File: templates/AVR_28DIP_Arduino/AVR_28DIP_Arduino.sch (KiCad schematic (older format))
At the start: 9 parts

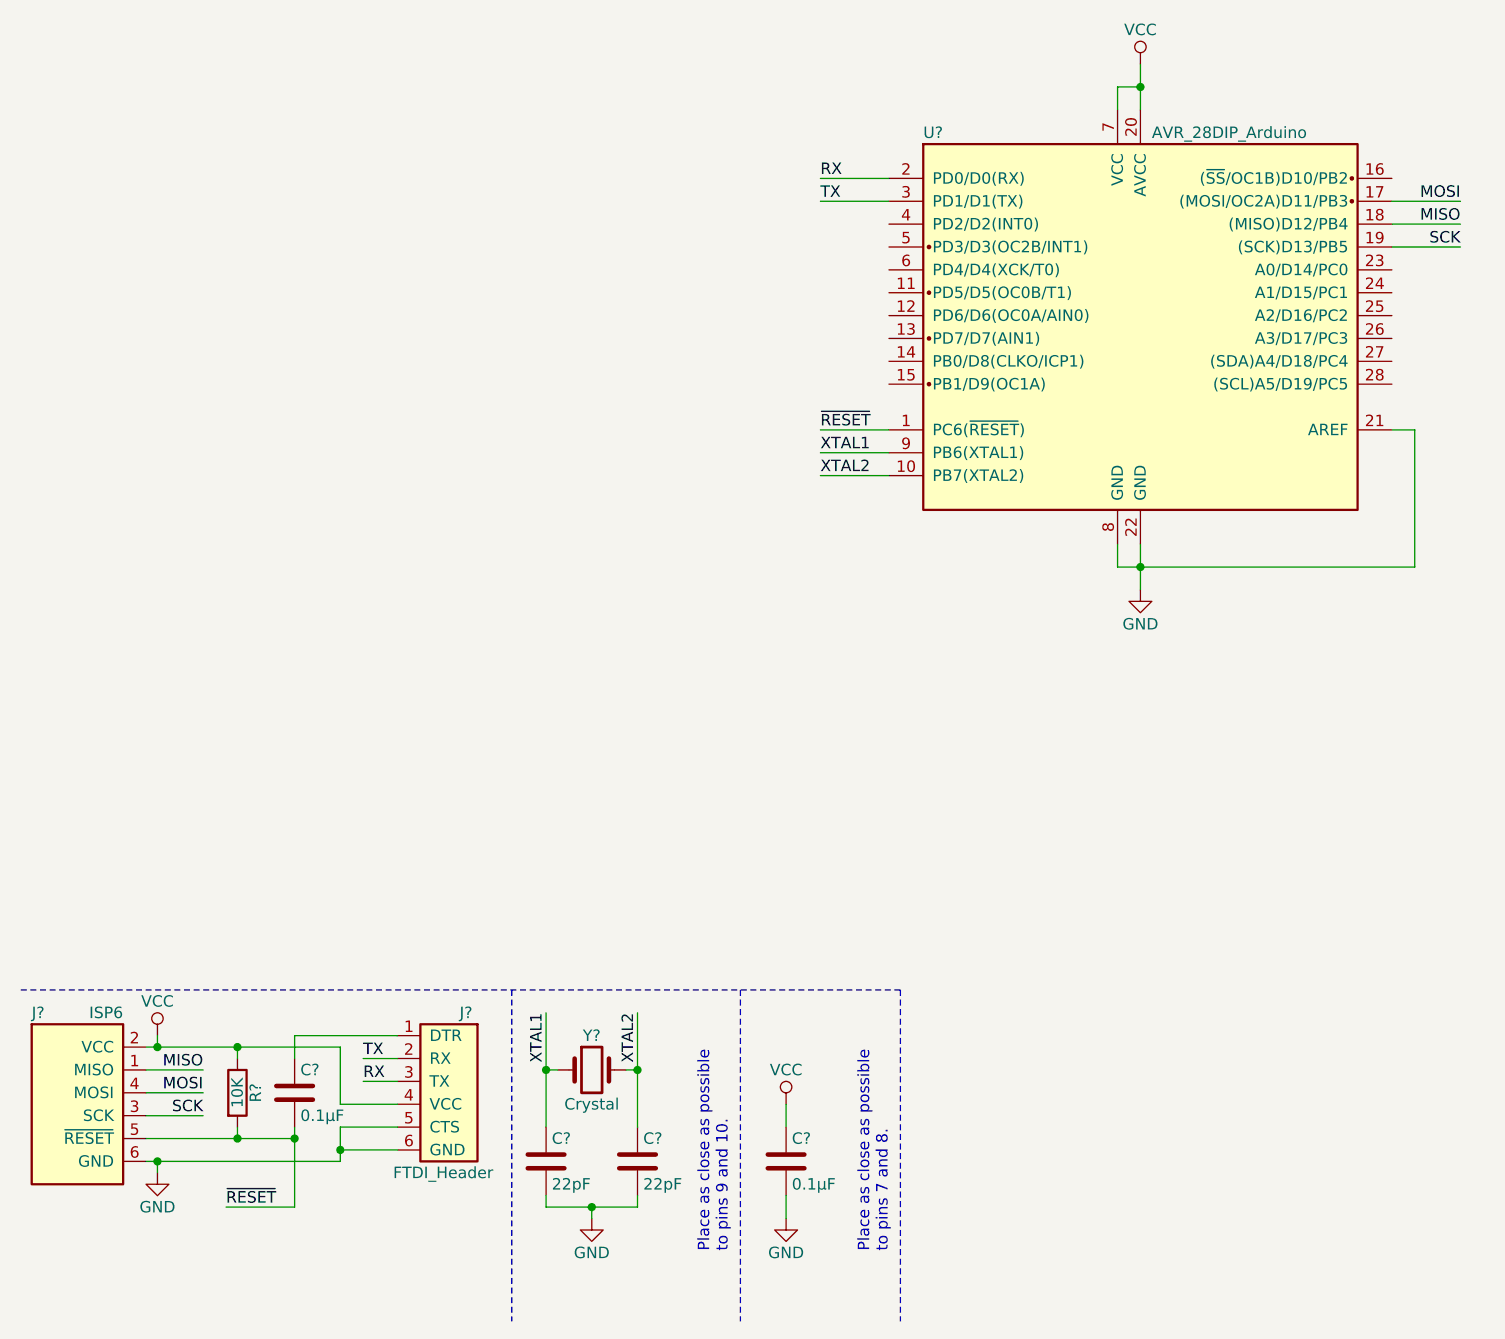
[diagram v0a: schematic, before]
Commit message: Add a capacitor between AREF and GND.  Also, make AREF Passive.
See this discussion:
https://forum.kicad.info/t/barebones-atmega328-circuit-and-the-conflict-between-pins-warning/10886
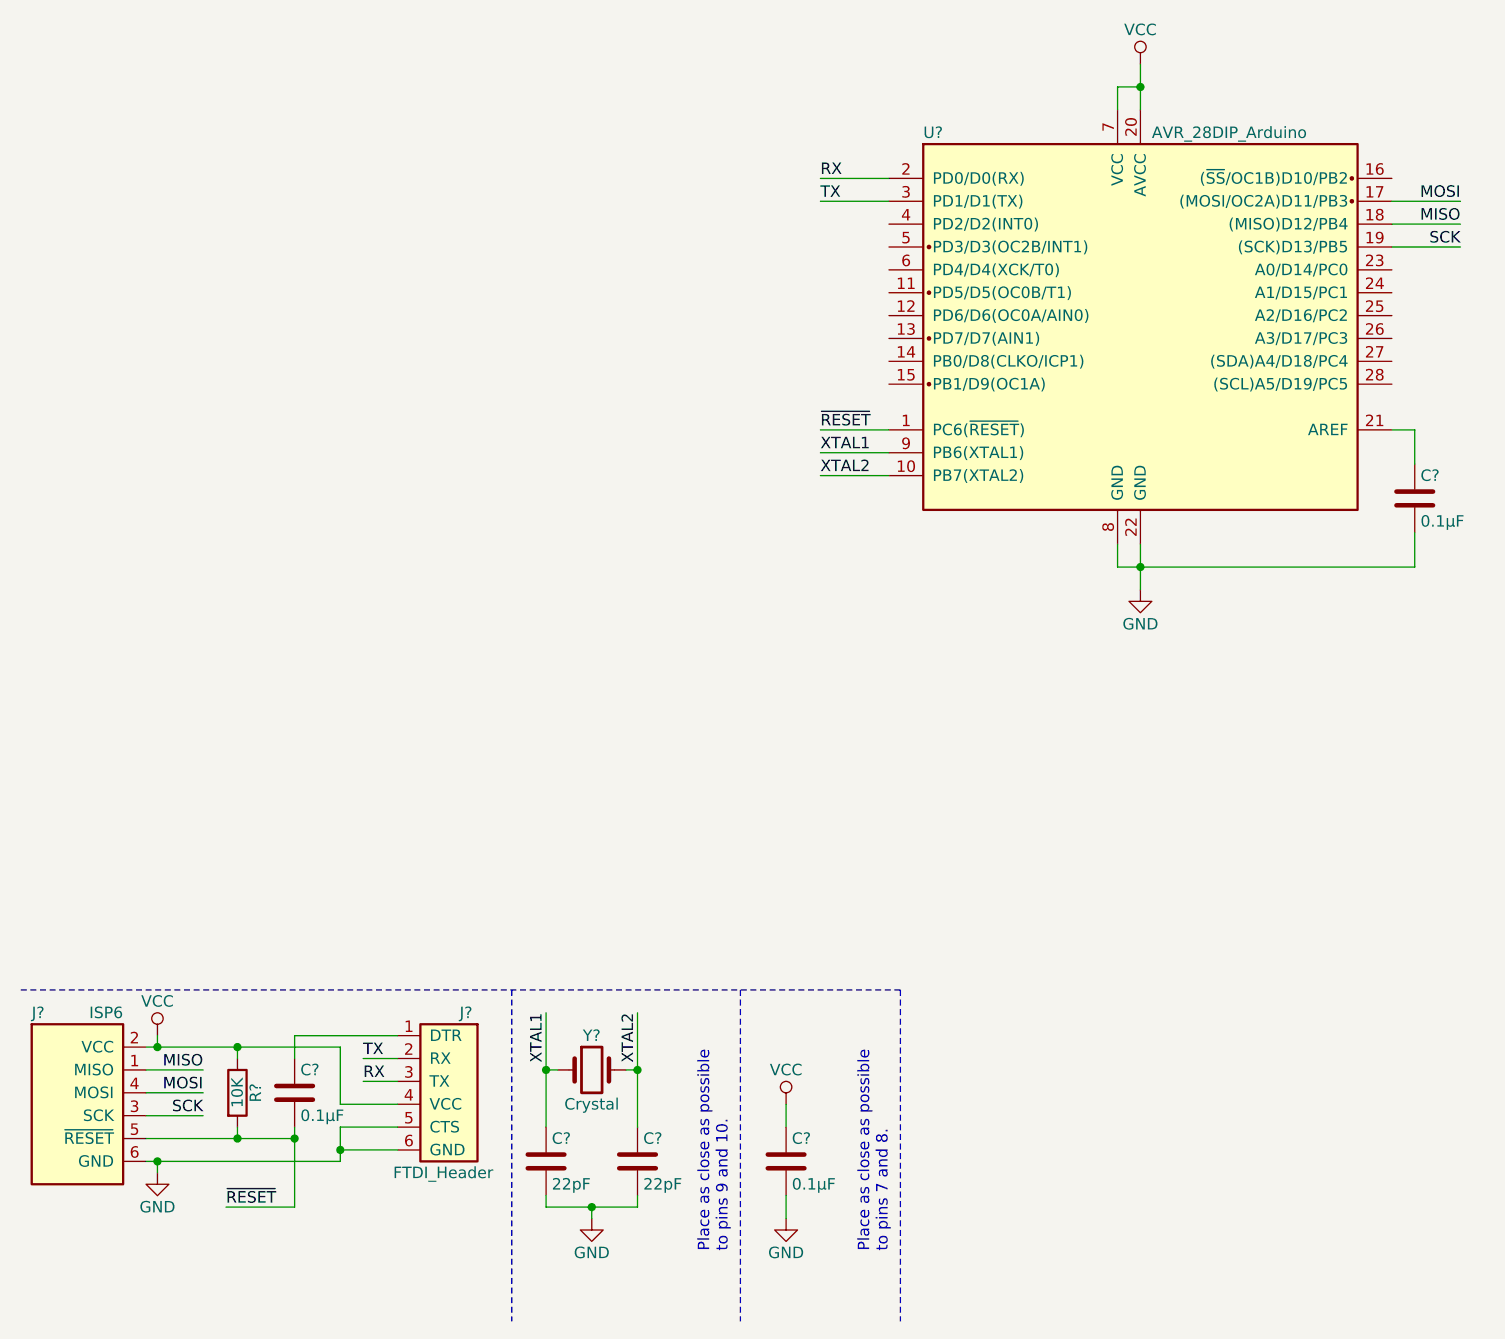
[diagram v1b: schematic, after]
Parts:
- added C?: 0.1μF, symbol C
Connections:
- net GND: now also C?.2; no longer U?.21 (AREF)
- new net: C?.1, U?.21 (AREF)
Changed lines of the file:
@@
 ~RESET
 Wire Wire Line
-	1050 6800 1100 6800
-Wire Wire Line
-	1100 6800 1450 6800
-Wire Wire Line
-	1450 6800 1900 6800
+	1050 6800 1900 6800
 Wire Wire Line
 	1100 6800 1100 6750
 Wire Wire Line
-	1050 7300 1100 7300
-Wire Wire Line
-	1100 7300 1900 7300
+	1900 7300 1050 7300
 Wire Wire Line
 	1100 7300 1100 7350
@@
 	2000 6950 2150 6950
 Wire Wire Line
-	1050 7200 1450 7200
-Wire Wire Line
-	1450 7200 1700 7200
+	1050 7200 1700 7200
 Wire Wire Line
 	1450 7200 1450 7150
@@
 Connection ~ 1100 6800
 Wire Wire Line
-	1700 7150 1700 7200
-Wire Wire Line
-	1700 7200 1700 7500
+	1700 7150 1700 7500
 Connection ~ 1450 7200
 Wire Wire Line
@@
 	2150 7150 1900 7150
 Wire Wire Line
-	1900 7150 1900 7250
-Wire Wire Line
-	1900 7250 1900 7300
+	1900 7150 1900 7300
 Connection ~ 1100 7300
 Wire Wire Line
@@
 	2800 7450 2800 7500
 Wire Wire Line
-	2800 7500 3000 7500
-Wire Wire Line
-	3000 7500 3200 7500
+	2800 7500 3200 7500
 Wire Wire Line
 	3200 7500 3200 7450
@@
 Connection ~ 3000 7500
 Wire Wire Line
-	2800 6650 2800 6900
-Wire Wire Line
-	2800 6900 2800 7150
+	2800 6650 2800 7150
 Wire Wire Line
 	2800 6900 2850 6900
@@
 	3150 6900 3200 6900
 Wire Wire Line
-	3200 6650 3200 6900
-Wire Wire Line
-	3200 6900 3200 7150
+	3200 6650 3200 7150
 Text Label 2800 6650 3    50   ~ 0
 XTAL1
@@
 $EndComp
 Wire Wire Line
-	5400 2700 5400 2600
-Wire Wire Line
-	5400 2600 5400 2500
+	5400 2500 5400 2700
 Wire Wire Line
 	5300 2700 5300 2600
@@
 Connection ~ 5400 2600
 Wire Wire Line
-	5400 4600 5400 4700
-Wire Wire Line
-	5400 4700 5400 4800
+	5400 4600 5400 4800
 Wire Wire Line
 	5300 4600 5300 4700
 Wire Wire Line
-	5300 4700 5400 4700
-Wire Wire Line
-	5400 4700 6600 4700
+	5300 4700 6600 4700
 Connection ~ 5400 4700
 Wire Wire Line
 	6500 4100 6600 4100
-Wire Wire Line
-	6600 4100 6600 4700
 Text Label 6800 3100 2    50   ~ 0
 MOSI
@@
 	1    0    0    -1
 $EndComp
+$Comp
+L C C?
+U 1 1 5B0980A7
+P 6600 4400
+F 0 "C?" H 6625 4500 50  0000 L CNN
+F 1 "0.1μF" H 6625 4300 50  0000 L CNN
+F 2 "" H 6638 4250 50  0001 C CNN
+F 3 "" H 6600 4400 50  0001 C CNN
+	1    6600 4400
+	1    0    0    -1
+$EndComp
+Wire Wire Line
+	6600 4100 6600 4250
+Wire Wire Line
+	6600 4700 6600 4550
 $EndSCHEMATC
